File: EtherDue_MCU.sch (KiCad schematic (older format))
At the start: 31 parts, among them IC201 ATSAM3X8E, SW201 ERASE, SW202 RESET, U202 FDN340P, U203 LMV358IPWR, X201 TXC 7A 12MHz 18pF, X202 ABS07L 32.768kHz

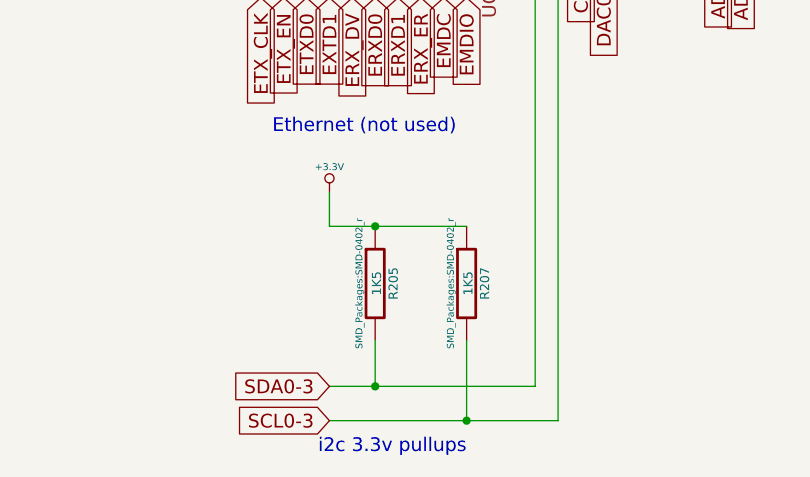
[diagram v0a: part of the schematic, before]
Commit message: exported cmp-file from PCB and back imported it into the schematic. then exported BOM with kicad2csvbom tool
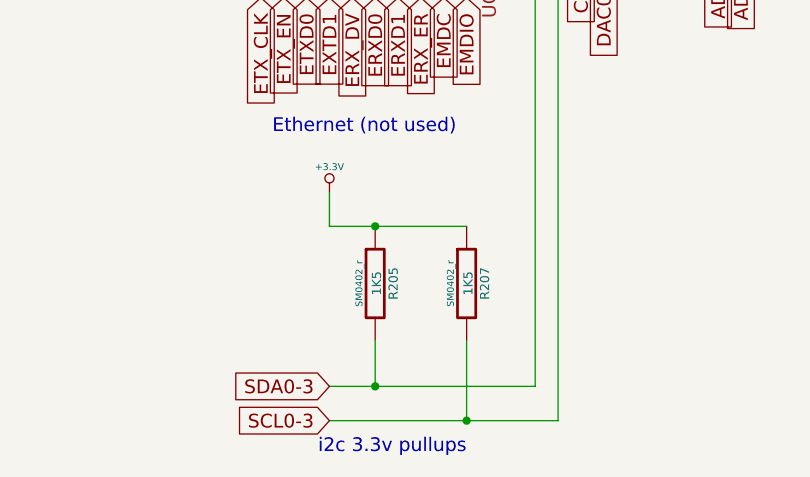
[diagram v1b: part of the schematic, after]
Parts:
- C201, C202, C203, C204, C205, C206, C207, C208: footprint SMD_Packages:SMD-0402_c -> SM0402
- D201, D202, D203, D204: footprint LEDs:LED-0603 -> zeilhofer:LED-0603
- IC201: footprint SMD_Packages:TQFP-144 -> TQFP144
- R201, R202, R203, R204, R205, R207: footprint SMD_Packages:SMD-0402_r -> SM0402_r
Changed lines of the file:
@@
 F 0 "IC201" H 5900 3050 50  0000 C CNN
 F 1 "ATSAM3X8E" H 6050 2950 50  0000 C CNN
-F 2 "SMD_Packages:TQFP-144" H 6500 3550 50  0001 C CNN
+F 2 "TQFP144" H 6500 3550 50  0001 C CNN
 F 3 "DOCUMENTATION" H 6650 3650 50  0001 C CNN
 	1    7900 5650
@@
 F 0 "C208" H 13050 2050 50  0000 L CNN
 F 1 "100nF" H 13050 1850 50  0000 L CNN
-F 2 "SMD_Packages:SMD-0402_c" H 13000 1950 60  0001 C CNN
+F 2 "SM0402" H 13000 1950 60  0001 C CNN
 F 3 "" H 13000 1950 60  0001 C CNN
 	1    13000 1950
@@
 F 0 "D201" H 13800 6600 50  0000 C CNN
 F 1 "YELLOW" H 13800 6400 50  0000 C CNN
-F 2 "LEDs:LED-0603" H 13800 6500 60  0001 C CNN
+F 2 "zeilhofer:LED-0603" H 13800 6500 60  0001 C CNN
 F 3 "" H 13800 6500 60  0001 C CNN
 	1    13800 6500
@@
 F 0 "D202" H 13800 6900 50  0000 C CNN
 F 1 "YELLOW" H 13800 6700 50  0000 C CNN
-F 2 "LEDs:LED-0603" H 13800 6800 60  0001 C CNN
+F 2 "zeilhofer:LED-0603" H 13800 6800 60  0001 C CNN
 F 3 "" H 13800 6800 60  0001 C CNN
 	1    13800 6800
@@
 F 0 "D204" H 14950 5600 50  0000 C CNN
 F 1 "YELLOW" H 14950 5400 50  0000 C CNN
-F 2 "LEDs:LED-0603" H 14950 5500 60  0001 C CNN
+F 2 "zeilhofer:LED-0603" H 14950 5500 60  0001 C CNN
 F 3 "" H 14950 5500 60  0001 C CNN
 	1    14950 5500
@@
 F 0 "D203" H 14950 5250 50  0000 C CNN
 F 1 "GREEN" H 14950 5050 50  0000 C CNN
-F 2 "LEDs:LED-0603" H 14950 5150 60  0001 C CNN
+F 2 "zeilhofer:LED-0603" H 14950 5150 60  0001 C CNN
 F 3 "" H 14950 5150 60  0001 C CNN
 	1    14950 5150
@@
 F 0 "R201" V 3480 5500 50  0000 C CNN
 F 1 "6k8 1%" V 3400 5500 50  0000 C CNN
-F 2 "SMD_Packages:SMD-0402_r" H 3400 5500 60  0001 C CNN
+F 2 "SM0402_r" H 3400 5500 60  0001 C CNN
 F 3 "" H 3400 5500 60  0001 C CNN
 	1    3400 5500
@@
 F 0 "C205" H 3850 5600 50  0000 L CNN
 F 1 "22pF" H 3850 5400 50  0000 L CNN
-F 2 "SMD_Packages:SMD-0402_c" H 3800 5500 60  0001 C CNN
+F 2 "SM0402" H 3800 5500 60  0001 C CNN
 F 3 "" H 3800 5500 60  0001 C CNN
 	1    3800 5500
@@
 F 0 "R202" V 5280 4100 50  0000 C CNN
 F 1 "39R 1%" V 5200 4100 50  0000 C CNN
-F 2 "SMD_Packages:SMD-0402_r" H 5200 4100 60  0001 C CNN
+F 2 "SM0402_r" H 5200 4100 60  0001 C CNN
 F 3 "" H 5200 4100 60  0001 C CNN
 	1    5200 4100
@@
 F 0 "R203" V 5280 4300 50  0000 C CNN
 F 1 "39R 1%" V 5200 4300 50  0000 C CNN
-F 2 "SMD_Packages:SMD-0402_r" H 5200 4300 60  0001 C CNN
+F 2 "SM0402_r" H 5200 4300 60  0001 C CNN
 F 3 "" H 5200 4300 60  0001 C CNN
 	1    5200 4300
@@
 F 0 "C204" H 3250 5000 50  0000 L CNN
 F 1 "22pF_NM" V 3300 4500 50  0000 L CNN
-F 2 "SMD_Packages:SMD-0402_c" H 3200 4900 60  0001 C CNN
+F 2 "SM0402" H 3200 4900 60  0001 C CNN
 F 3 "" H 3200 4900 60  0001 C CNN
 	1    3200 4900
@@
 F 0 "C203" H 3250 4250 50  0000 L CNN
 F 1 "22pF_NM" V 3300 3750 50  0000 L CNN
-F 2 "SMD_Packages:SMD-0402_c" H 3200 4150 60  0001 C CNN
+F 2 "SM0402" H 3200 4150 60  0001 C CNN
 F 3 "" H 3200 4150 60  0001 C CNN
 	1    3200 4150
@@
 F 0 "C202" H 3250 3850 50  0000 L CNN
 F 1 "22pF" H 3250 3650 50  0000 L CNN
-F 2 "SMD_Packages:SMD-0402_c" H 3200 3750 60  0001 C CNN
+F 2 "SM0402" H 3200 3750 60  0001 C CNN
 F 3 "" H 3200 3750 60  0001 C CNN
 	1    3200 3750
@@
 F 0 "C201" H 3250 2800 50  0000 L CNN
 F 1 "22pF" H 3250 2600 50  0000 L CNN
-F 2 "SMD_Packages:SMD-0402_c" H 3200 2700 60  0001 C CNN
+F 2 "SM0402" H 3200 2700 60  0001 C CNN
 F 3 "" H 3200 2700 60  0001 C CNN
 	1    3200 2700
@@
 F 0 "C206" H 6350 1550 50  0000 L CNN
 F 1 "100nF" H 6350 1350 50  0000 L CNN
-F 2 "SMD_Packages:SMD-0402_c" H 6300 1450 60  0001 C CNN
+F 2 "SM0402" H 6300 1450 60  0001 C CNN
 F 3 "" H 6300 1450 60  0001 C CNN
 	1    6300 1450
@@
 F 0 "C207" H 7050 1450 50  0000 L CNN
 F 1 "100nF" H 6900 1250 50  0000 L CNN
-F 2 "SMD_Packages:SMD-0402_c" H 7150 1350 60  0001 C CNN
+F 2 "SM0402" H 7150 1350 60  0001 C CNN
 F 3 "" H 7150 1350 60  0001 C CNN
 	1    7150 1350
@@
 F 0 "R204" V 6830 2300 50  0000 C CNN
 F 1 "100K" V 6750 2300 50  0000 C CNN
-F 2 "SMD_Packages:SMD-0402_r" H 6750 2300 60  0001 C CNN
+F 2 "SM0402_r" H 6750 2300 60  0001 C CNN
 F 3 "" H 6750 2300 60  0001 C CNN
 	1    6750 2300
@@
 F 0 "R205" V 6980 10150 40  0000 C CNN
 F 1 "1K5" V 6907 10151 40  0000 C CNN
-F 2 "SMD_Packages:SMD-0402_r" V 6830 10150 30  0000 C CNN
+F 2 "SM0402_r" V 6830 10150 30  0000 C CNN
 F 3 "~" H 6900 10150 30  0000 C CNN
 	1    6900 10150
@@
 F 0 "R207" V 7380 10150 40  0000 C CNN
 F 1 "1K5" V 7307 10151 40  0000 C CNN
-F 2 "SMD_Packages:SMD-0402_r" V 7230 10150 30  0000 C CNN
+F 2 "SM0402_r" V 7230 10150 30  0000 C CNN
 F 3 "~" H 7300 10150 30  0000 C CNN
 	1    7300 10150

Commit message: Updates im Zuge des Tutorials
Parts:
- added C209: 10nF, FT:C0402, symbol C
- added C210: 10uF, FT:SM0603_Capa, symbol C
- added R209: 33R, Resistors_SMD:R_0402, symbol R
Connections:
- net +3.3V: now also C209.1, C210.1
- net /MASTER-RESET: now also C209.2
- net GND: now also C210.2
- net at C201.2, X201.1: now also R209.2; no longer IC201.35 (XOUT)
- new net: IC201.35 (XOUT), R209.1
